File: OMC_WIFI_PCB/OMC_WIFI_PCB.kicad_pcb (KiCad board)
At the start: 2 copper layers, 18 parts, among them J1 ESP32_Left, J10 Control_ACS712, J11 Control_ZMPT101B, J12 Power_Out_Load, J2 ESP32_Right, J3 Power_In, J4 Switch, J5 Pins_FT232R, J6 Line_Relay, J7 Control_Relay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

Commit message: Actualización PCB
+ Medidas de ZMPT101B
+ Medidas Módulo Relay
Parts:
- removed R2: 2k, Resistor_SMD:R_1812_4532Metric_Pad1.30x3.40mm_HandSolder
- removed R3: 1k, Resistor_SMD:R_2010_5025Metric_Pad1.40x2.65mm_HandSolder
- removed U1: LM741, Package_DIP:DIP-8_W10.16mm
- J4: footprint Connector_Wire:SolderWire-0.75sqmm_1x02_P7mm_D1.25mm_OD3.5mm -> Connector_Wire:SolderWire-0.75sqmm_1x03_P4.8mm_D1.25mm_OD2.3mm
- J6, J7: footprint Connector_Wire:SolderWire-0.75sqmm_1x03_P4.8mm_D1.25mm_OD2.3mm -> TerminalBlock:TerminalBlock_bornier-3_P5.08mm
- moved J7 185.5 mm to (667.5, -901.5), turned to 180 degrees
- moved J8 182.3 mm to (632.2, -941.0)
- moved J6 177.7 mm to (672.3, -937.3), turned to 180 degrees
- moved J12 154.9 mm to (711.2, -970.3), turned to 180 degrees
- moved J3 146.4 mm to (599.8, -978.8), turned to 180 degrees
- moved PS1 113.1 mm to (589.2, -943.0)
- moved J9 111.4 mm to (611.2, -940.5)
- moved J11 110.4 mm to (618.6, -896.0)
- moved J4 109.4 mm to (589.2, -957.8), turned to 180 degrees
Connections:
- J4 pad 1: LINE -> +5V
- J7 pad 1: Net-(J7-Pad1) -> D32_RELAY
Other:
- net class 220V LC added: clearance 1, trace_width 2, via_dia 1.2, via_drill 0.6
- net class Default: clearance 0.2 -> 0.3; trace_width 0.25 -> 0.3; via_dia 0.8 -> 1.2; via_drill 0.4 -> 0.6
- rule pad_to_mask_clearance: 0 -> 0.05
- rule trace_clearance: 0.2 -> 0.3
- board text added: "Mdulo Relay SLA-05VDC-SL-C"

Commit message: Actualización PCB
+ Medidas ACS712
- Conexión 5V al switch
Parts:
- moved J10 184.1 mm to (637.7, -915.8)
- moved J2 84.1 mm to (592.4, -876.6), turned to 90 degrees
- moved J1 78.3 mm to (592.4, -872.0), turned to 90 degrees
- moved D1 68.2 mm to (776.6, -928.5)
- moved J5 68.2 mm to (741.3, -948.3)
- moved R1 68.2 mm to (701.3, -929.9)
- moved J8 0.89 mm to (632.4, -940.1)

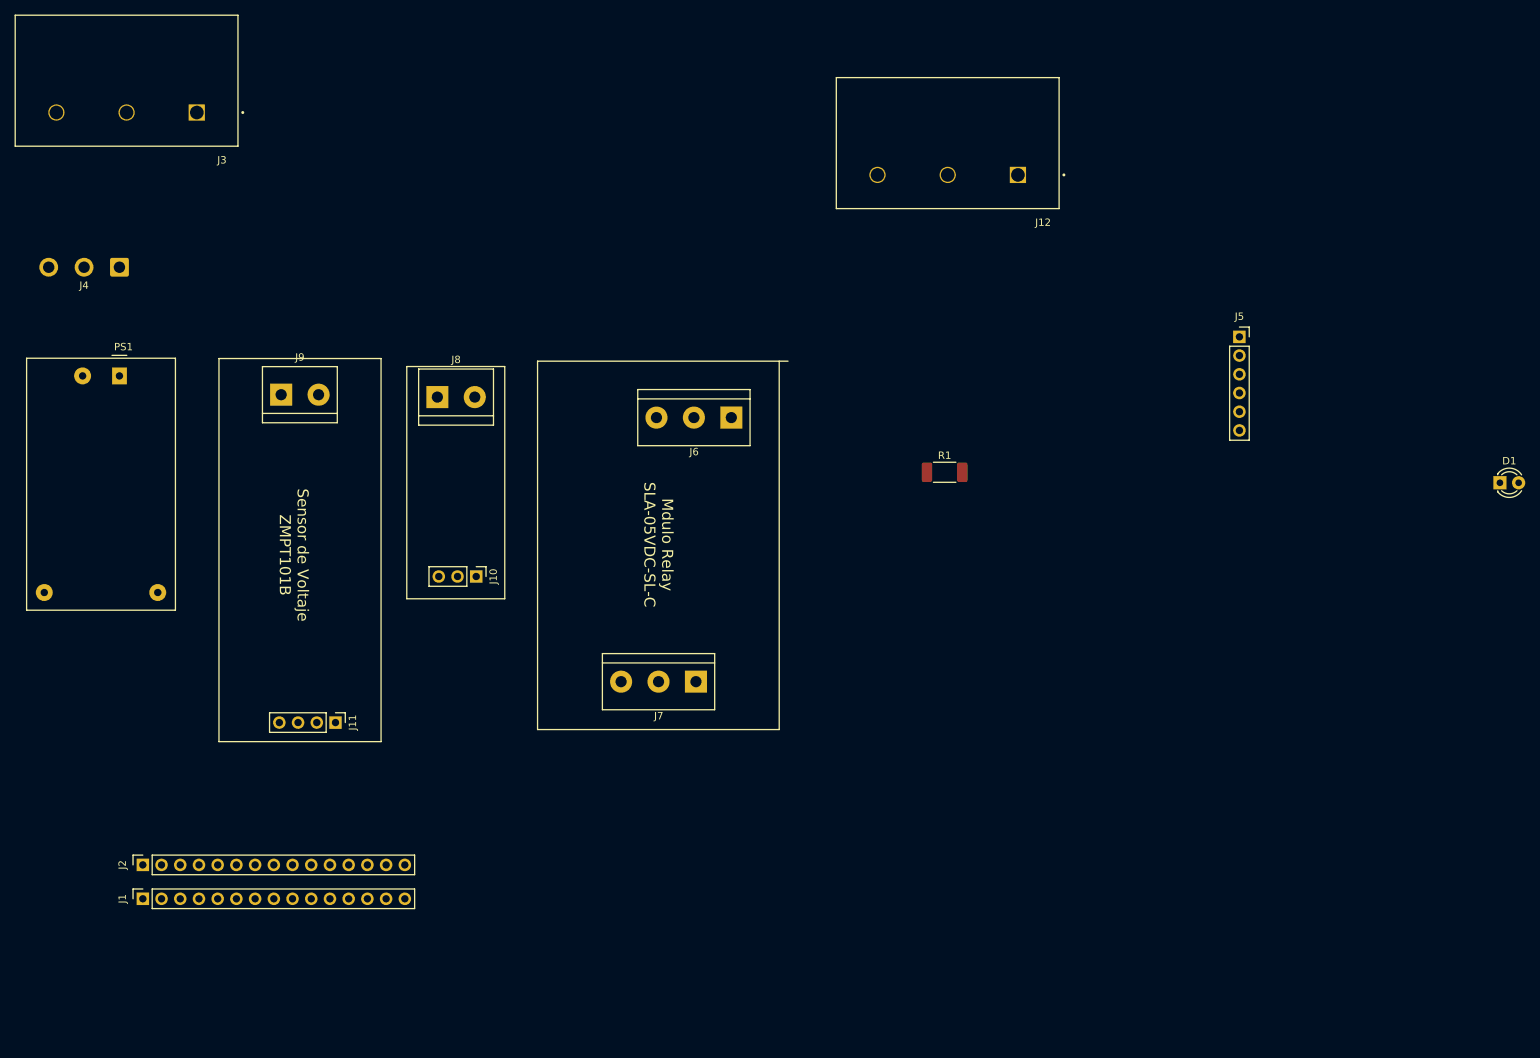
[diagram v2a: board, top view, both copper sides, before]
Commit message: Actualización PCB
+ Pistas digitales
> Modificación de Tags
> Rediseño de la PCB
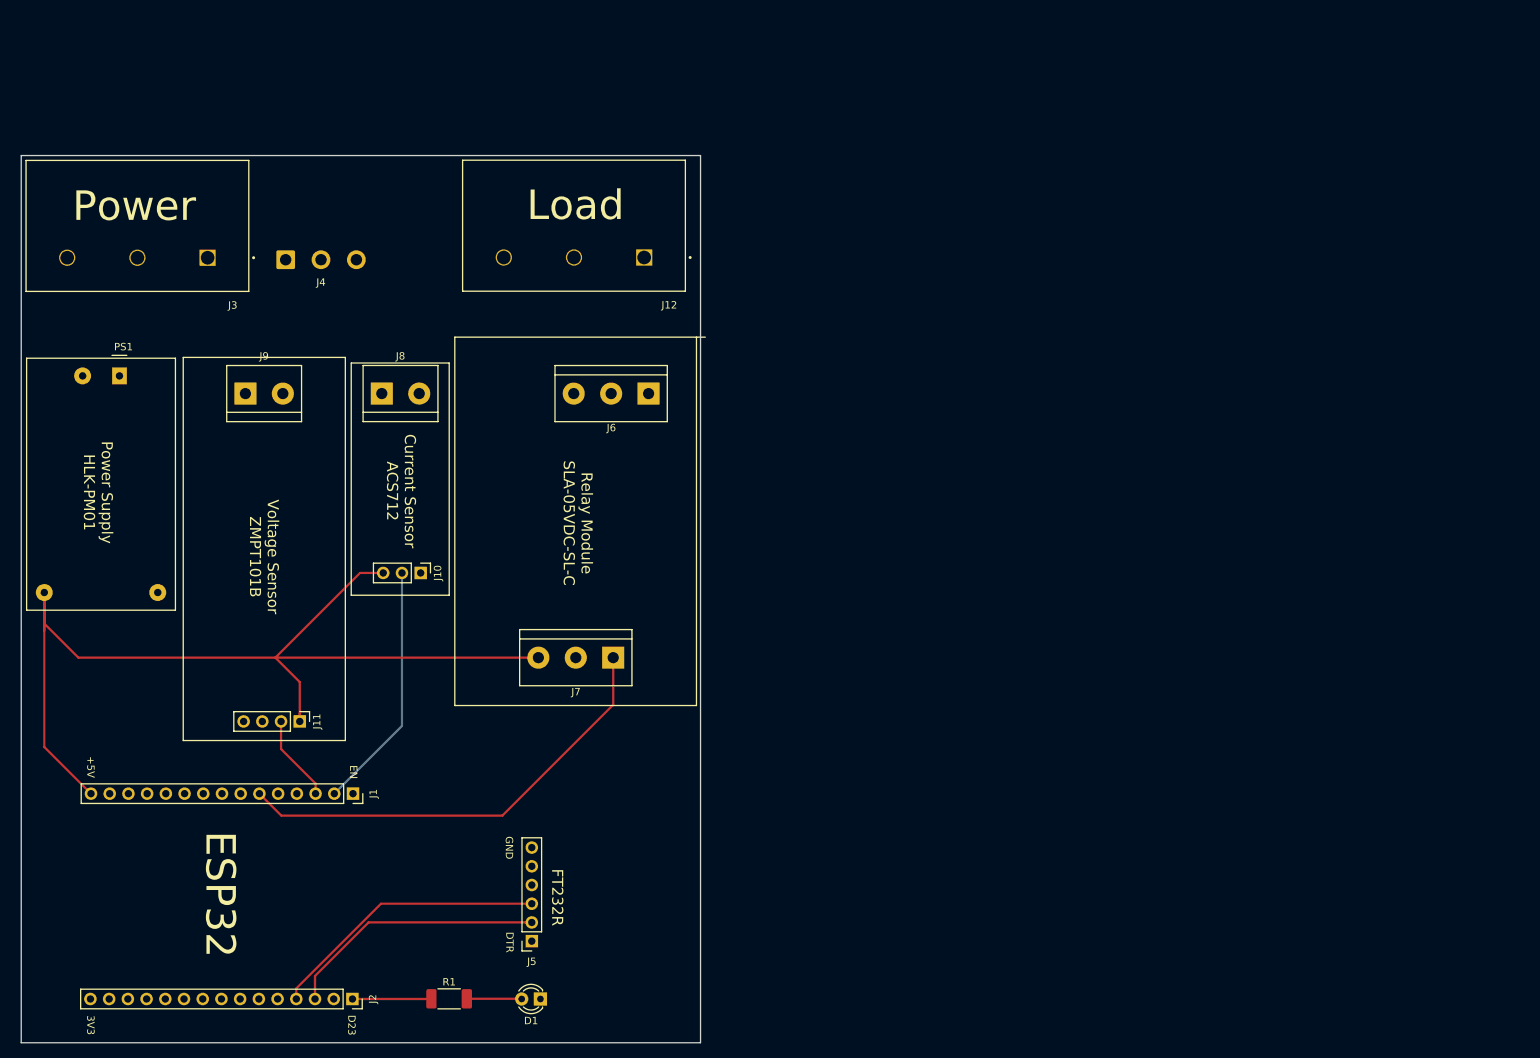
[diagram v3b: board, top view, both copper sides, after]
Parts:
- moved D1 147.9 mm to (646.4, -858.4), turned to 180 degrees
- moved J5 126.3 mm to (645.2, -866.3), turned to 180 degrees
- moved R1 98.1 mm to (634.0, -858.5)
- moved J12 51.9 mm to (660.5, -959.1)
- moved J2 33.8 mm to (620.9, -858.4), turned to 270 degrees
- moved J1 31.9 mm to (620.9, -886.3), turned to 270 degrees
- moved J4 22.6 mm to (611.8, -958.8), turned to 0 degrees
- moved J3 19.8 mm to (601.2, -959.0)
- moved J7 11.7 mm to (656.3, -904.8)
- moved J6 11.7 mm to (661.1, -940.6)
- moved J10 7.56 mm to (630.1, -916.3)
- moved J8 7.56 mm to (624.9, -940.6)
- moved J11 4.85 mm to (613.7, -896.1)
- moved J9 4.85 mm to (606.4, -940.6)
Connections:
- net I_ACS renamed PHASE
- J1 pad 10: D27_LED -> D27
- J1 pad 2: VP_ZMPT -> VP_ACS
- J1 pad 3: VN_ACS -> VN_ZMPT
- J10 pad 2: VN_ACS -> VP_ACS
- J11 pad 2: VP_ZMPT -> VN_ZMPT
- J12 pad 1: Net-(J12-Pad1) -> GND
- J12 pad 2: NO -> COM
- J12 pad 3: GND -> LINE
- J2 pad 1: D23 -> D23_LED
- J3 pad 1: LINE -> Net-(J3-Pad1)
- J4 pad 1: +5V -> Net-(J4-Pad1)
- J4 pad 2: Net-(J12-Pad1) -> Net-(J3-Pad1)
- J5 pad 2: RX0 -> TX0
- J5 pad 3: TX0 -> RX0
- J8 pad 2: COM -> NO
- R1 pad 1: D27_LED -> D23_LED
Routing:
- net +5V: track 0.00 -> 142.5 mm
- net D32_RELAY: track 0.00 -> 61.9 mm
- net RX0: track 0.00 -> 38.2 mm
- net TX0: track 0.00 -> 35.6 mm
- net VP_ACS: track 0.00 -> 33.8 mm
- net VN_ZMPT: track 0.00 -> 11.7 mm
- net D23_LED: track 0.00 -> 10.7 mm
- net Net-(D1-Pad2): track 0.00 -> 7.46 mm
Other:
- board outline added: 92.2 x 120.4 mm
- net class 220V HC added: clearance 1, trace_width 4, via_dia 1.2, via_drill 0.6
- board text added: "+5V"
- board text added: "3V3"
- board text added: "Current Sensor ACS712"
- board text added: "D23"
- board text added: "DTR"
- board text added: "EN"
- board text added: "ESP32"
- board text added: "FT232R"
- board text added: "GND"
- board text added: "Load"
- board text added: "Power"
- board text added: "Power Supply HLK-PM01"
- board text added: "Relay Module SLA-05VDC-SL-C"
- board text added: "Voltage Sensor ZMPT101B"
- board text removed: "Mdulo Relay SLA-05VDC-SL-C"
- board text removed: "Sensor de Voltaje ZMPT101B"

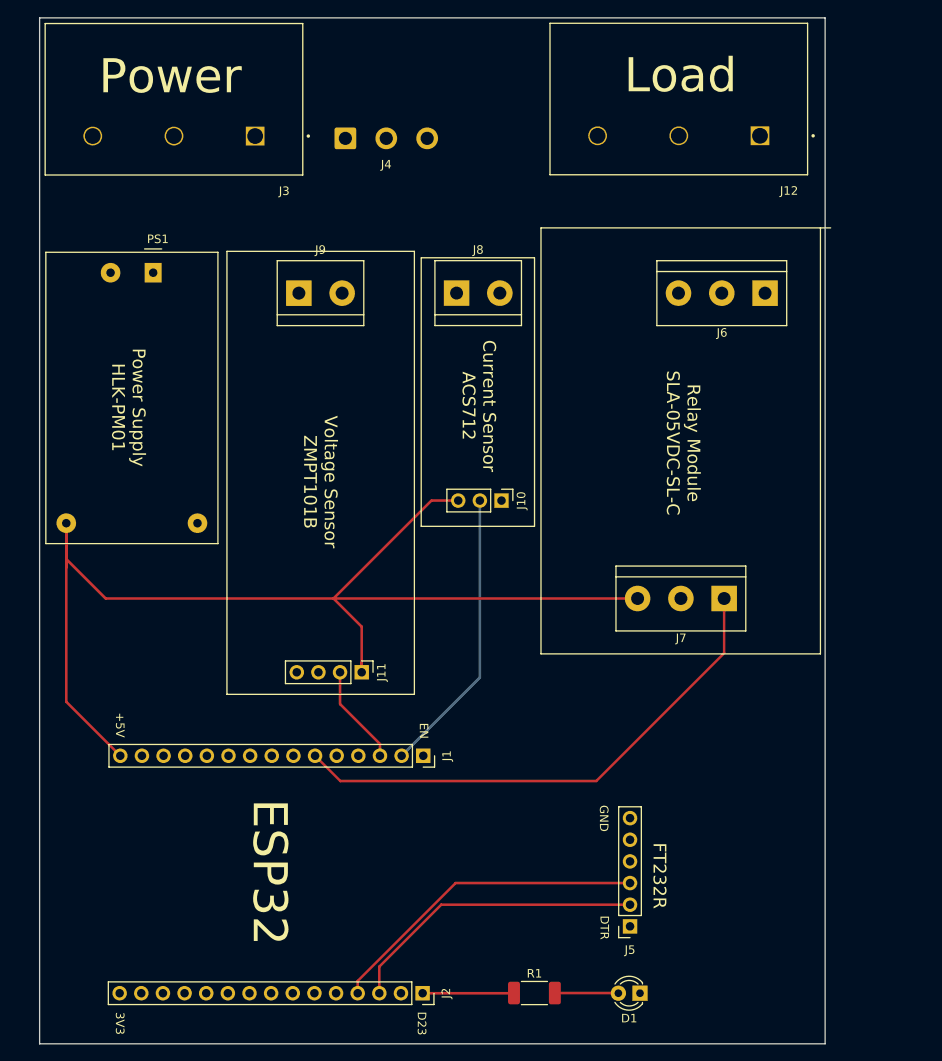
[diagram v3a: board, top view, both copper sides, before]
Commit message: Actualización PCB
+Plano de Tierra
> Rediseño PCB para utilizar un solo conector
> Redistribución de pistas
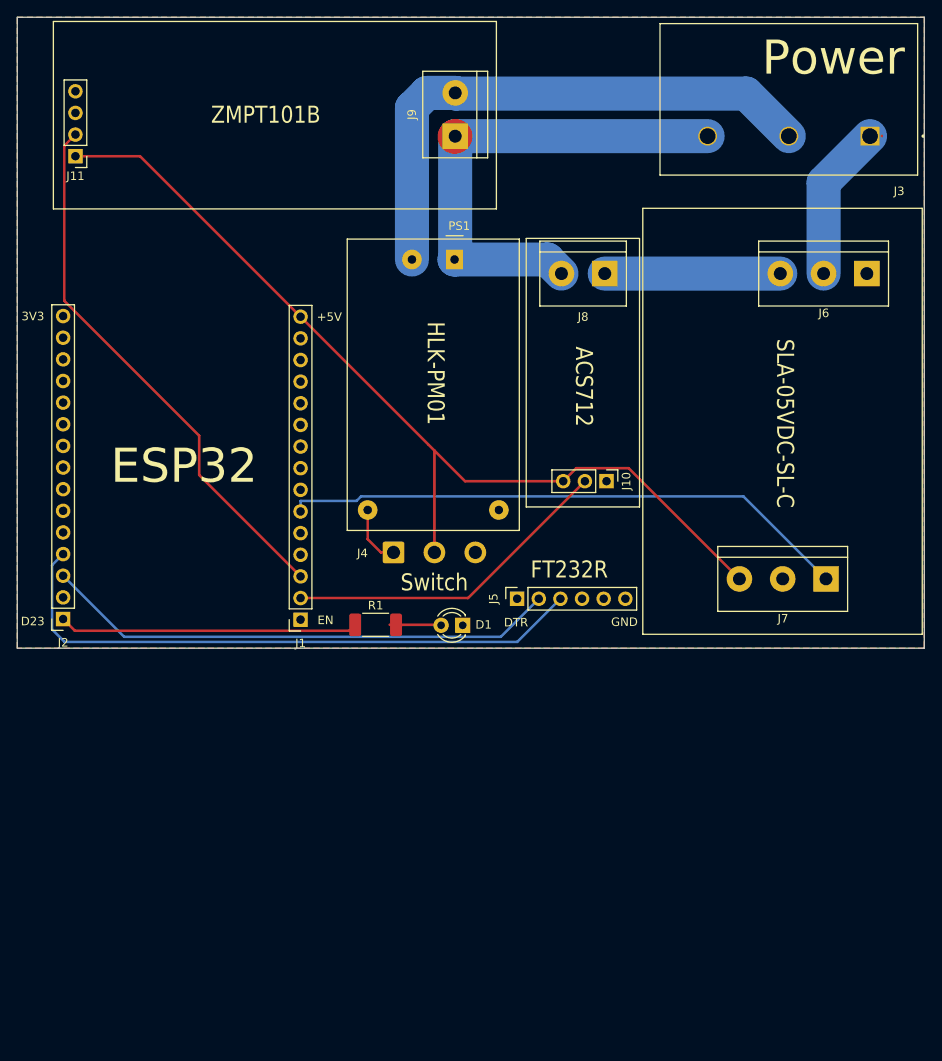
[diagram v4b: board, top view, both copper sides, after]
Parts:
- removed J12: Power_Out_Load, 6PCV-03-006:TE_5-1437652-4
- moved J3 72.2 mm to (673.4, -959.0)
- moved J11 69.3 mm to (580.1, -956.7), turned to 180 degrees
- moved J2 60.9 mm to (578.7, -902.4), turned to 180 degrees
- moved J4 48.9 mm to (617.5, -910.2)
- moved D1 47.9 mm to (625.6, -901.6)
- moved R1 47.1 mm to (615.4, -901.7)
- moved J5 40.7 mm to (632.0, -904.7), turned to 90 degrees
- moved PS1 35.4 mm to (624.6, -944.5)
- moved J9 26.0 mm to (624.7, -959.0), turned to 90 degrees
- moved J1 21.5 mm to (606.5, -902.3), turned to 180 degrees
- moved J8 17.5 mm to (642.2, -942.9), turned to 180 degrees
- moved J10 12.5 mm to (642.5, -918.5)
- moved J7 12.2 mm to (668.2, -907.1)
- moved J6 12.2 mm to (673.0, -942.9)
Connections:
- J3 pad 1: Net-(J3-Pad1) -> COM
- J3 pad 2: PHASE -> NEUTRAL
- J3 pad 3: GND -> LINE
- J4 pad 2: Net-(J3-Pad1) -> +5V
- J4 pad 3: LINE -> GND
- J8 pad 1: PHASE -> NO
- J8 pad 2: NO -> LINE
- J9 pad 2: PHASE -> NEUTRAL
- PS1 pad 2: PHASE -> NEUTRAL
- PS1 pad 4: +5V -> Net-(J4-Pad1)
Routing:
- net NEUTRAL: track 0.00 -> 64.9 mm
- net LINE: track 0.00 -> 57.5 mm
- net VN_ZMPT: track 11.7 -> 63.9 mm
- net RX0: track 38.2 -> 71.7 mm
- net +5V: track 142.5 -> 111.7 mm
- net TX0: track 35.6 -> 60.6 mm
- net D23_LED: track 10.7 -> 35.1 mm
- net NO: track 0.00 -> 20.6 mm
- net COM: track 0.00 -> 18.4 mm
- net Net-(J4-Pad1): track 0.00 -> 7.10 mm
- net VP_ACS: track 33.8 -> 39.1 mm
- net D32_RELAY: track 61.9 -> 67.1 mm
- net Net-(D1-Pad2): track 7.46 -> 5.40 mm
- added copper zone on B.Cu, net GND
- added copper zone on F.Cu, net GND
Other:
- board size 92.2 x 120.4 mm -> 106.5 x 74.1 mm
- board text added: "ACS712"
- board text added: "HLK-PM01"
- board text added: "SLA-05VDC-SL-C"
- board text added: "Switch"
- board text added: "ZMPT101B"
- board text removed: "Current Sensor ACS712"
- board text removed: "Load"
- board text removed: "Power Supply HLK-PM01"
- board text removed: "Relay Module SLA-05VDC-SL-C"
- board text removed: "Voltage Sensor ZMPT101B"

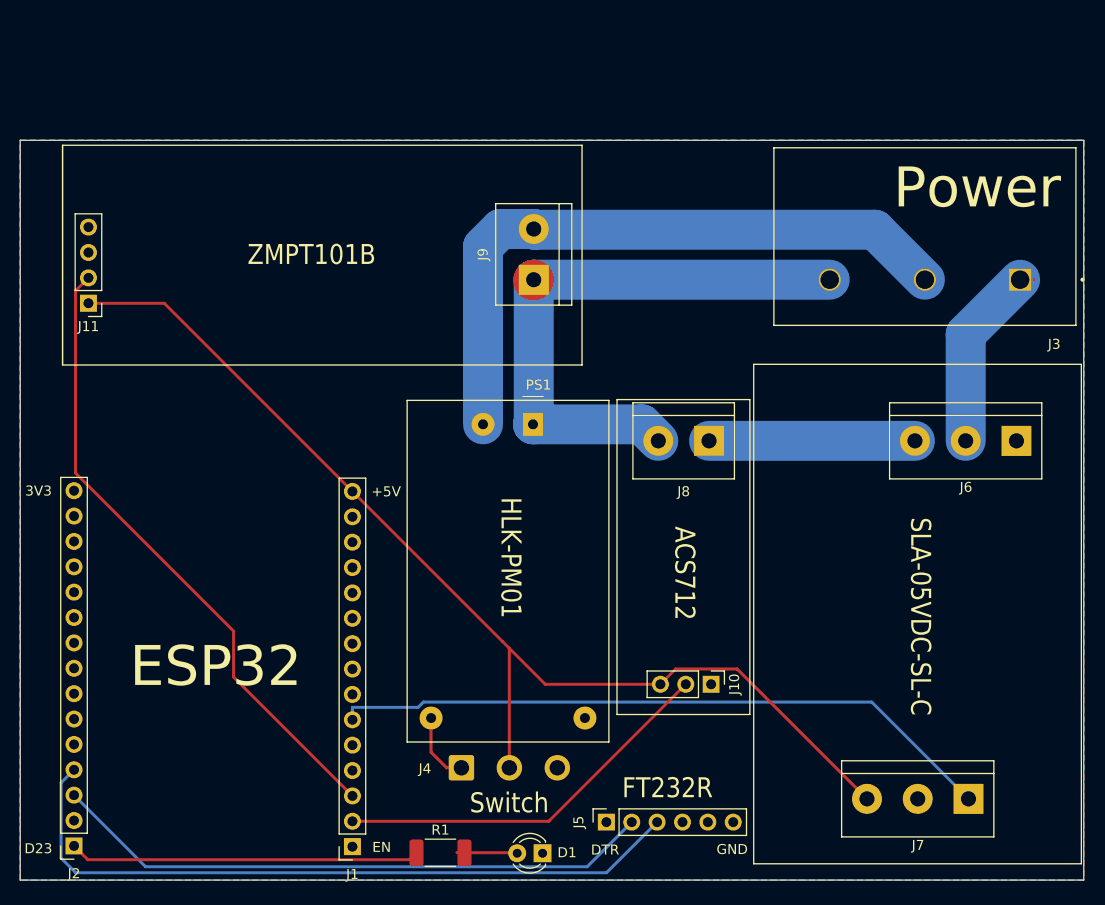
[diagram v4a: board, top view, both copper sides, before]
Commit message: Actualización PCB
+ Jumper para ACS
+ Fusible
> Rediseño de la PCB
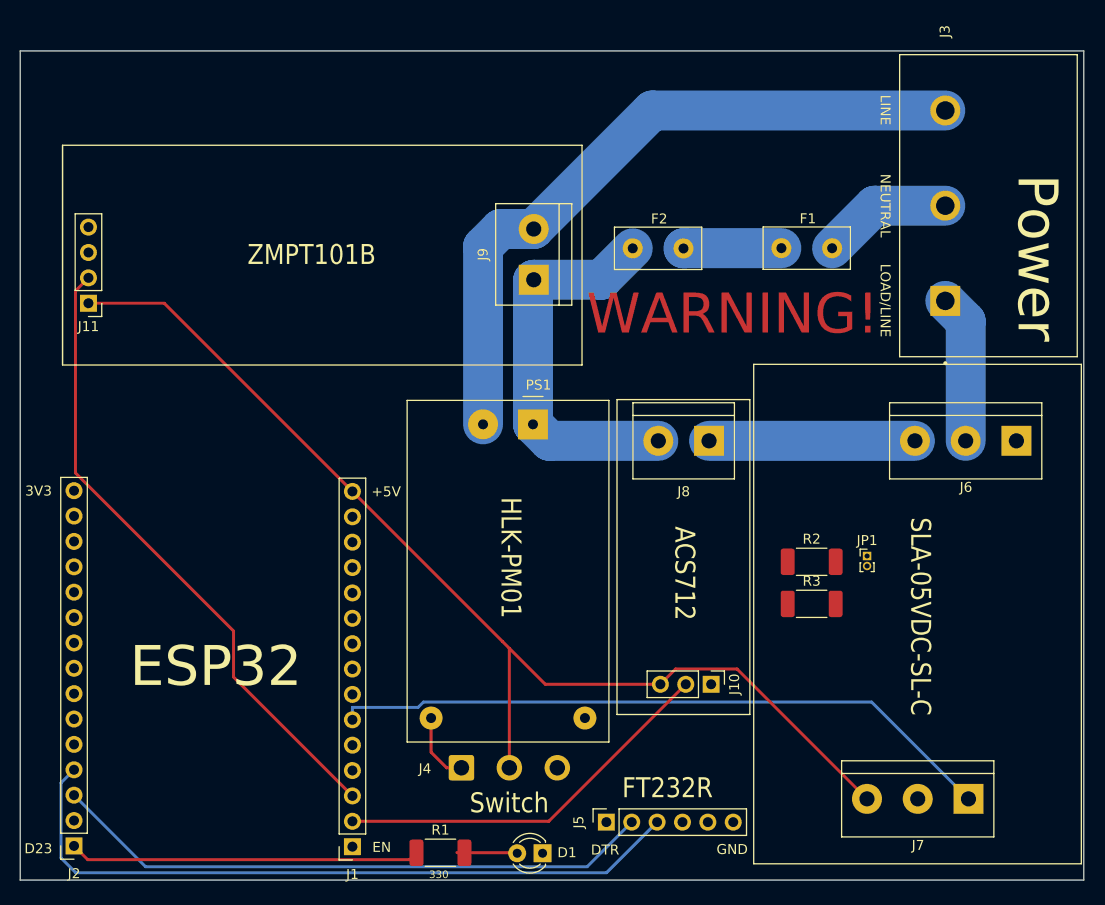
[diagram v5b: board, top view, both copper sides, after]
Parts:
- added F1: Fuse, Fuse:Fuse_Littelfuse_395Series, F.Cu at (649.5, -962.2)
- added F2: Fuse, Fuse:Fuse_Littelfuse_395Series, F.Cu at (634.6, -962.2)
- added JP1: Jumper, Connector_PinHeader_1.00mm:PinHeader_1x02_P1.00mm_Vertical, F.Cu at (658.1, -931.4)
- added R2: 10K, Resistor_SMD:R_2010_5025Metric_Pad1.40x2.65mm_HandSolder, F.Cu at (652.5, -930.8)
- added R3: 20k, Resistor_SMD:R_2010_5025Metric_Pad1.40x2.65mm_HandSolder, F.Cu at (652.5, -926.6)
- moved J3 7.78 mm to (665.9, -956.9), turned to 90 degrees
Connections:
- J10 pad 2: VP_ACS -> Net-(J10-Pad2)
- J3 pad 2: NEUTRAL -> Net-(F1-Pad2)
- J3 pad 3: LINE -> NEUTRAL
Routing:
- net LINE: track 57.5 -> 38.9 mm
- net Net-(F1-Pad2): track 0.00 -> 13.1 mm
- net Net-(F1-Pad1): track 0.00 -> 9.81 mm
- net NEUTRAL: track 64.9 -> 69.7 mm
- net COM: track 18.4 -> 14.9 mm
- removed copper zone on B.Cu, net GND
- removed copper zone on F.Cu, net GND
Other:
- board size 106.5 x 74.1 mm -> 106.5 x 83 mm
- board text added: "330"
- board text added: "LINE"
- board text added: "LOAD/LINE"
- board text added: "NEUTRAL"
- board text added: "WARNING!"
